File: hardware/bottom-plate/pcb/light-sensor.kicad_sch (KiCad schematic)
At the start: 4 parts

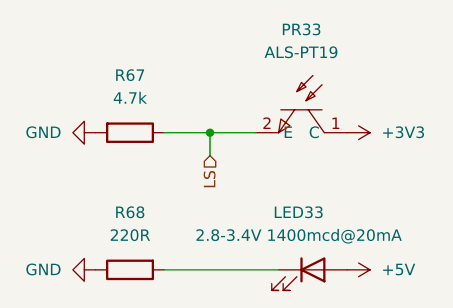
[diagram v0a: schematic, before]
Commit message: fixed line sensor positions
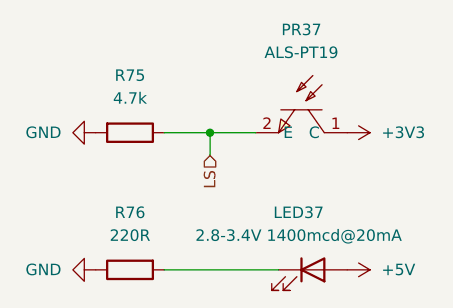
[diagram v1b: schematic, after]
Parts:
- renumbered LED33 to LED37, PR33 to PR37, R67 to R75, R68 to R76
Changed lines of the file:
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@@
 		(dnp no)
 		(fields_autoplaced yes)
-		(property "Reference" "R67"
+		(property "Reference" "R75"
 			(at 160.02 50.8 90)
 			(effects
@@
 		(dnp no)
 		(fields_autoplaced yes)
-		(property "Reference" "PR33"
+		(property "Reference" "PR37"
 			(at 179.07 45.72 90)
 			(effects
@@
 		(dnp no)
 		(fields_autoplaced yes)
-		(property "Reference" "#PWR0216"
+		(property "Reference" "#PWR0232"
 			(at 180.34 72.39 0)
 			(effects
@@
 		(dnp no)
 		(fields_autoplaced yes)
-		(property "Reference" "#PWR0215"
+		(property "Reference" "#PWR0231"
 			(at 180.34 57.15 0)
 			(effects
@@
 		(dnp no)
 		(fields_autoplaced yes)
-		(property "Reference" "LED33"
+		(property "Reference" "LED37"
 			(at 178.7525 66.04 0)
 			(effects
@@
 		(dnp no)
 		(fields_autoplaced yes)
-		(property "Reference" "#PWR0214"
+		(property "Reference" "#PWR0230"
 			(at 149.86 72.39 0)
 			(effects
@@
 		(dnp no)
 		(fields_autoplaced yes)
-		(property "Reference" "#PWR0213"
+		(property "Reference" "#PWR0229"
 			(at 149.86 57.15 0)
 			(effects
@@
 		(dnp no)
 		(fields_autoplaced yes)
-		(property "Reference" "R68"
+		(property "Reference" "R76"
 			(at 160.02 66.04 90)
 			(effects

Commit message: completed bottom pcb
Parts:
- renumbered LED37 to LED33, PR37 to PR33, R75 to R67, R76 to R68
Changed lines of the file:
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@@
 		(dnp no)
 		(fields_autoplaced yes)
-		(property "Reference" "R75"
+		(property "Reference" "R67"
 			(at 160.02 50.8 90)
 			(effects
@@
 		(dnp no)
 		(fields_autoplaced yes)
-		(property "Reference" "PR37"
+		(property "Reference" "PR33"
 			(at 179.07 45.72 90)
 			(effects
@@
 		(dnp no)
 		(fields_autoplaced yes)
-		(property "Reference" "#PWR0232"
+		(property "Reference" "#PWR0216"
 			(at 180.34 72.39 0)
 			(effects
@@
 		(dnp no)
 		(fields_autoplaced yes)
-		(property "Reference" "#PWR0231"
+		(property "Reference" "#PWR0215"
 			(at 180.34 57.15 0)
 			(effects
@@
 		(dnp no)
 		(fields_autoplaced yes)
-		(property "Reference" "LED37"
+		(property "Reference" "LED33"
 			(at 178.7525 66.04 0)
 			(effects
@@
 		(dnp no)
 		(fields_autoplaced yes)
-		(property "Reference" "#PWR0230"
+		(property "Reference" "#PWR0214"
 			(at 149.86 72.39 0)
 			(effects
@@
 		(dnp no)
 		(fields_autoplaced yes)
-		(property "Reference" "#PWR0229"
+		(property "Reference" "#PWR0213"
 			(at 149.86 57.15 0)
 			(effects
@@
 		(dnp no)
 		(fields_autoplaced yes)
-		(property "Reference" "R76"
+		(property "Reference" "R68"
 			(at 160.02 66.04 90)
 			(effects
